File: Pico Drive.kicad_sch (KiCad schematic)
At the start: 23 parts, among them J1 Conn_01x06_Male, J2 Conn_01x08, J3 Conn_01x02_Male, J4 Conn_01x02_Male, SW1 Reset, U1 Pico, U2 74AXP1T45GWH, U3 74AHCT1G125, U4 OLED-I2C-Module-Aliexpress

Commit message: Shifted bits around, ran power, added cutout
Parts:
- added H1, H2, H3, H4: MountingHole, MountingHole:MountingHole_2.2mm_M2, symbol Mechanical:MountingHole
- SW1: footprint Button_Switch_THT:SW_PUSH-12mm -> Button_Switch_THT:SW_PUSH_6mm
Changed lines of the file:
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@@
     (pin "1")
+  )
+  (symbol (lib_id "Mechanical:MountingHole") (at 107.95 54.61 0) (unit 1)
+    (in_bom yes) (on_board yes) (fields_autoplaced)
+    (property "Reference" "H2" (id 0) (at 110.49 53.7753 0)
+      (effects (font (size 1.27 1.27)) (justify left))
+    )
+    (property "Value" "MountingHole" (id 1) (at 110.49 56.3122 0)
+      (effects (font (size 1.27 1.27)) (justify left))
+    )
+    (property "Footprint" "MountingHole:MountingHole_2.2mm_M2" (id 2) (at 107.95 54.61 0)
+      (effects (font (size 1.27 1.27)) hide)
+    )
+    (property "Datasheet" "~" (id 3) (at 107.95 54.61 0)
+      (effects (font (size 1.27 1.27)) hide)
+    )
   )
   (symbol (lib_id "power:GND") (at 71.12 57.15 90) (unit 1)
@@
     (pin "4")
   )
+  (symbol (lib_id "Mechanical:MountingHole") (at 88.9 54.61 0) (unit 1)
+    (in_bom yes) (on_board yes) (fields_autoplaced)
+    (property "Reference" "H1" (id 0) (at 91.44 53.7753 0)
+      (effects (font (size 1.27 1.27)) (justify left))
+    )
+    (property "Value" "MountingHole" (id 1) (at 91.44 56.3122 0)
+      (effects (font (size 1.27 1.27)) (justify left))
+    )
+    (property "Footprint" "MountingHole:MountingHole_2.2mm_M2" (id 2) (at 88.9 54.61 0)
+      (effects (font (size 1.27 1.27)) hide)
+    )
+    (property "Datasheet" "~" (id 3) (at 88.9 54.61 0)
+      (effects (font (size 1.27 1.27)) hide)
+    )
+  )
   (symbol (lib_id "Switch:SW_Push") (at 22.86 182.245 90) (unit 1)
     (in_bom yes) (on_board yes) (fields_autoplaced)
@@
       (effects (font (size 1.27 1.27)) (justify right))
     )
-    (property "Footprint" "Button_Switch_THT:SW_PUSH-12mm" (id 2) (at 17.78 182.245 0)
+    (property "Footprint" "Button_Switch_THT:SW_PUSH_6mm" (id 2) (at 17.78 182.245 0)
       (effects (font (size 1.27 1.27)) hide)
     )
@@
     (pin "1")
     (pin "2")
+  )
+  (symbol (lib_id "Mechanical:MountingHole") (at 88.9 59.69 0) (unit 1)
+    (in_bom yes) (on_board yes) (fields_autoplaced)
+    (property "Reference" "H3" (id 0) (at 91.44 58.8553 0)
+      (effects (font (size 1.27 1.27)) (justify left))
+    )
+    (property "Value" "MountingHole" (id 1) (at 91.44 61.3922 0)
+      (effects (font (size 1.27 1.27)) (justify left))
+    )
+    (property "Footprint" "MountingHole:MountingHole_2.2mm_M2" (id 2) (at 88.9 59.69 0)
+      (effects (font (size 1.27 1.27)) hide)
+    )
+    (property "Datasheet" "~" (id 3) (at 88.9 59.69 0)
+      (effects (font (size 1.27 1.27)) hide)
+    )
+  )
+  (symbol (lib_id "Mechanical:MountingHole") (at 107.95 59.69 0) (unit 1)
+    (in_bom yes) (on_board yes) (fields_autoplaced)
+    (property "Reference" "H4" (id 0) (at 110.49 58.8553 0)
+      (effects (font (size 1.27 1.27)) (justify left))
+    )
+    (property "Value" "MountingHole" (id 1) (at 110.49 61.3922 0)
+      (effects (font (size 1.27 1.27)) (justify left))
+    )
+    (property "Footprint" "MountingHole:MountingHole_2.2mm_M2" (id 2) (at 107.95 59.69 0)
+      (effects (font (size 1.27 1.27)) hide)
+    )
+    (property "Datasheet" "~" (id 3) (at 107.95 59.69 0)
+      (effects (font (size 1.27 1.27)) hide)
+    )
   )
   (symbol (lib_id "Connector_Generic:Conn_01x03") (at 35.56 97.79 0) (unit 1)
@@
       (reference "D1") (unit 1) (value "LED") (footprint "LED_THT:LED_D5.0mm")
     )
+    (path "/6aaac48c-1084-4417-a5ba-7ef20c482d61"
+      (reference "H1") (unit 1) (value "MountingHole") (footprint "MountingHole:MountingHole_2.2mm_M2")
+    )
+    (path "/36716edf-5df6-475e-8e31-d4be639e19ec"
+      (reference "H2") (unit 1) (value "MountingHole") (footprint "MountingHole:MountingHole_2.2mm_M2")
+    )
+    (path "/702feb10-b0c8-409f-9d53-2d411bf5bcd2"
+      (reference "H3") (unit 1) (value "MountingHole") (footprint "MountingHole:MountingHole_2.2mm_M2")
+    )
+    (path "/72a812fd-69d5-499a-ae49-86d7d93a117e"
+      (reference "H4") (unit 1) (value "MountingHole") (footprint "MountingHole:MountingHole_2.2mm_M2")
+    )
     (path "/39882caa-95f6-44aa-91c3-f39af783c8e6"
       (reference "J1") (unit 1) (value "Conn_01x06_Male") (footprint "Connector_PinHeader_2.54mm:PinHeader_1x06_P2.54mm_Horizontal")
@@
     )
     (path "/6c8f0377-4b1d-4b1f-8f24-8c0f143dd748"
-      (reference "SW1") (unit 1) (value "Reset") (footprint "Button_Switch_THT:SW_PUSH-12mm")
+      (reference "SW1") (unit 1) (value "Reset") (footprint "Button_Switch_THT:SW_PUSH_6mm")
     )
     (path "/ed3c498f-b044-4833-8009-2bc5c40e76df"

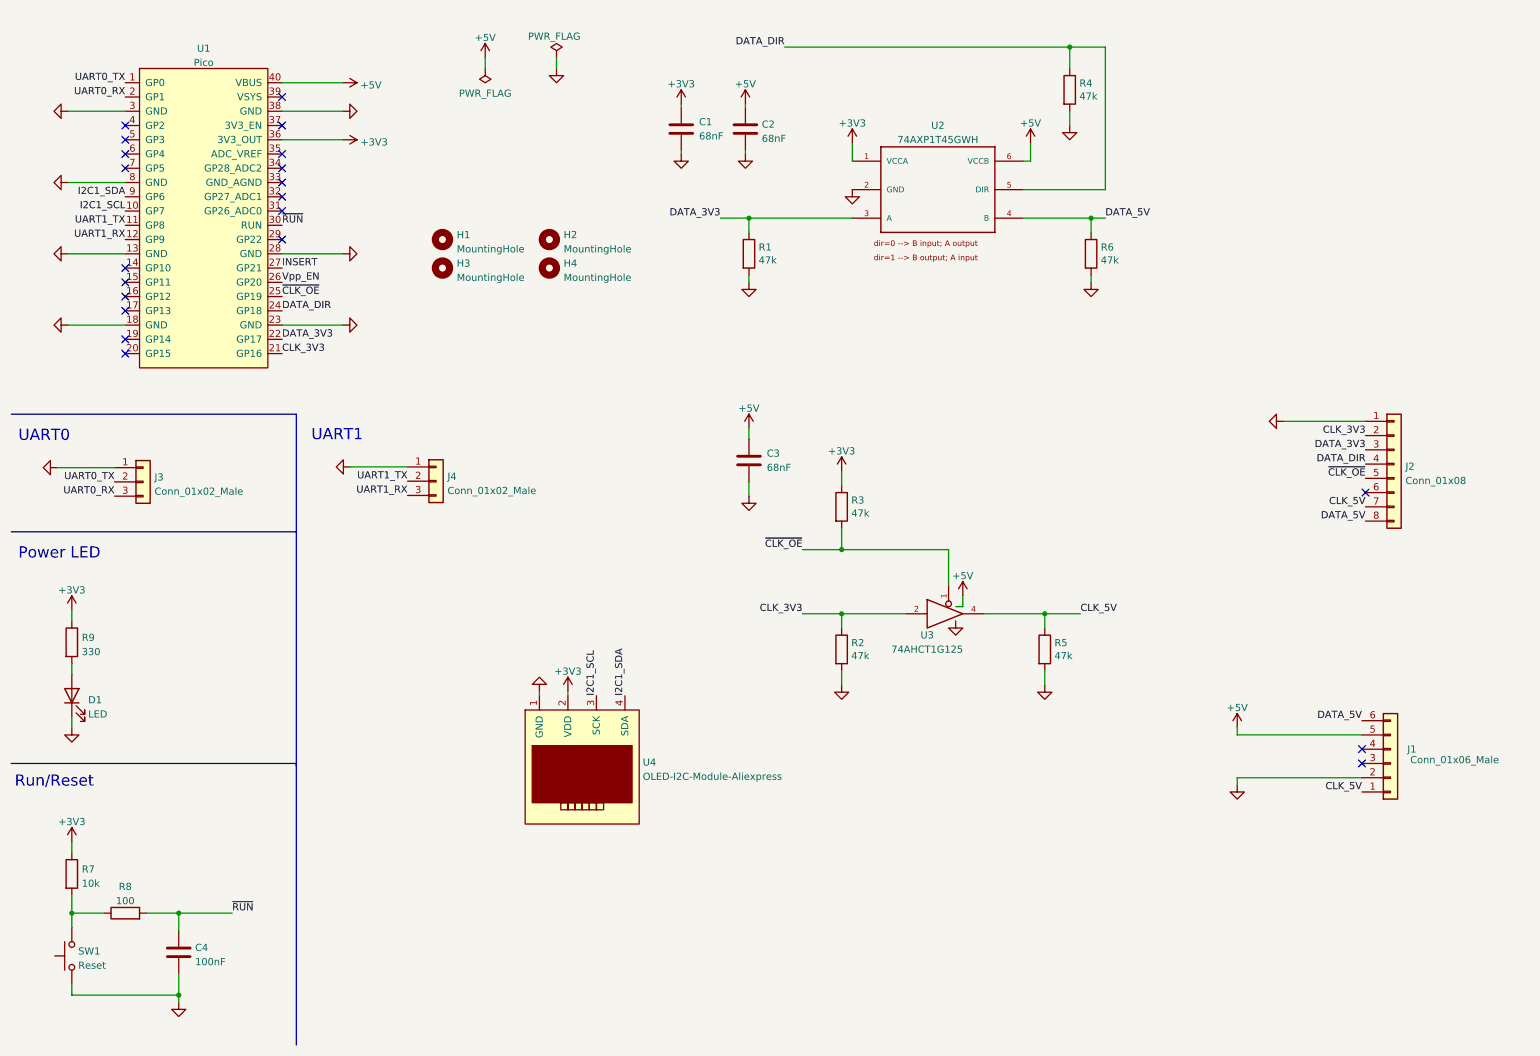
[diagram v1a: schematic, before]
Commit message: Swapped some TH for SMDs, fixed caps, tidied
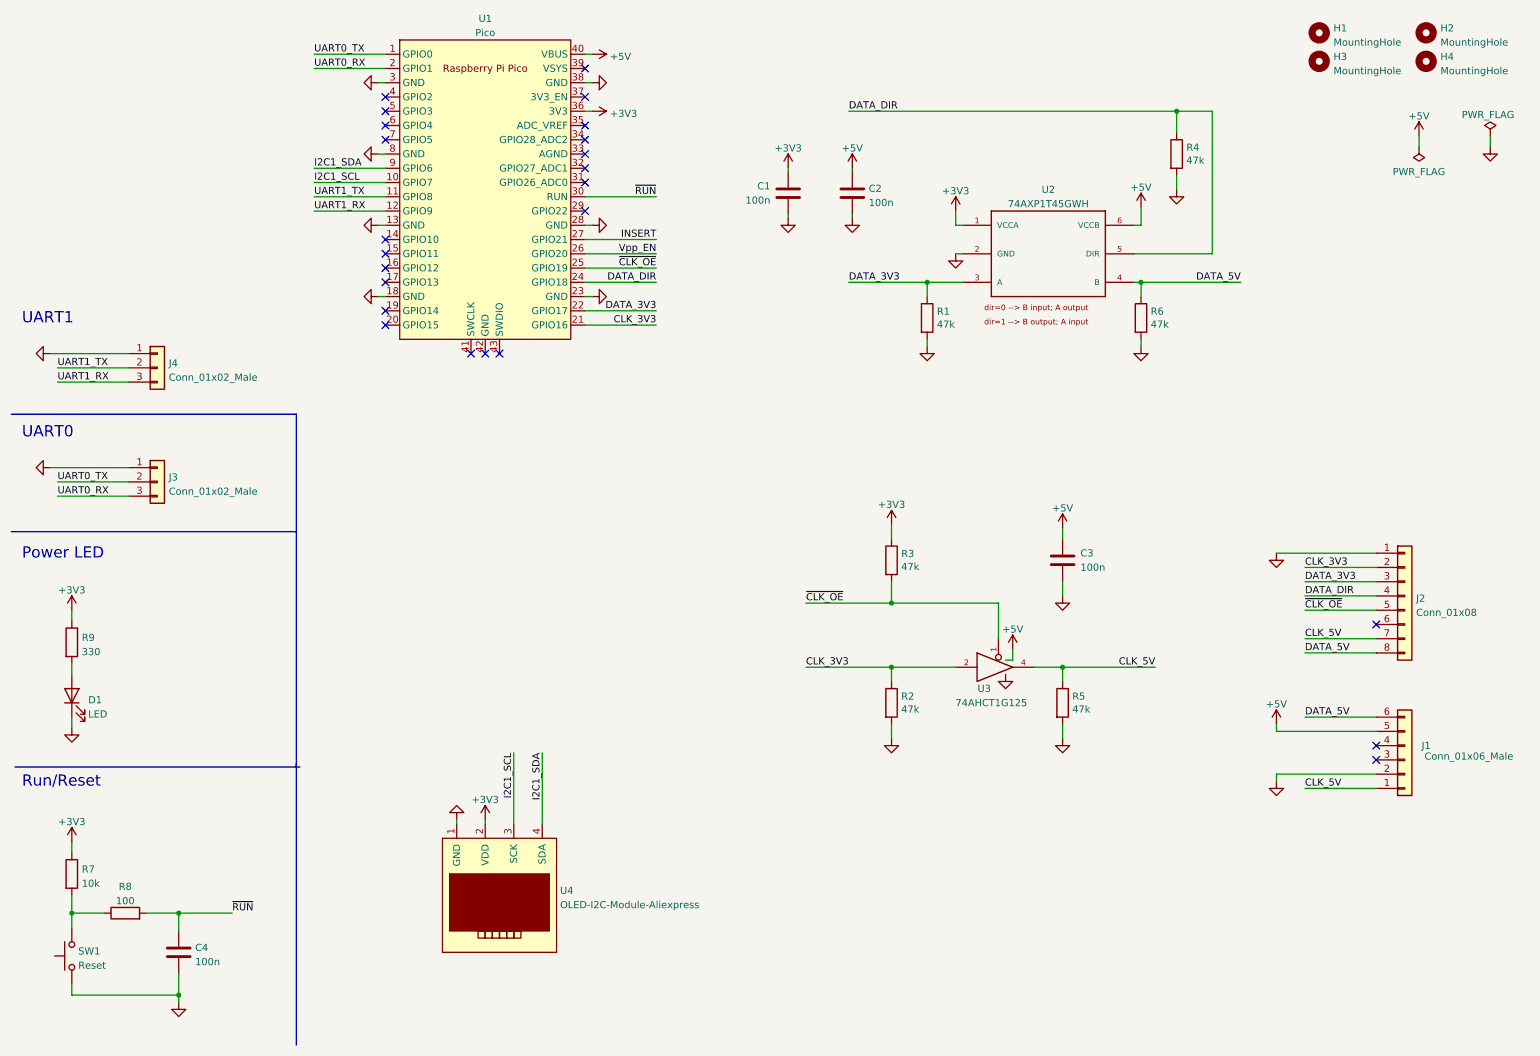
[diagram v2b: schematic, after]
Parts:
- removed U1: Pico, RPi_Pico:RPi_Pico_SMD_TH, symbol kiwih_kicad:raspberrypi-pico-module
- added U1: Pico, RP-Pico Libraries:RPi_Pico_SMD_TH, symbol MCU_RaspberryPi_and_Boards:Pico
- C1, C2, C3: value 68nF -> 100n; footprint Capacitor_THT:C_Disc_D4.3mm_W1.9mm_P5.00mm -> Capacitor_SMD:C_0402_1005Metric_Pad0.74x0.62mm_HandSolder
- C4: value 100nF -> 100n; footprint Capacitor_THT:C_Disc_D4.3mm_W1.9mm_P5.00mm -> Capacitor_SMD:C_0402_1005Metric_Pad0.74x0.62mm_HandSolder
- D1: footprint LED_THT:LED_D5.0mm -> LED_SMD:LED_0603_1608Metric_Pad1.05x0.95mm_HandSolder
- R1, R2, R3, R4, R5, R6, R7, R8, R9: footprint Resistor_THT:R_Axial_DIN0204_L3.6mm_D1.6mm_P7.62mm_Horizontal -> Resistor_SMD:R_0402_1005Metric_Pad0.72x0.64mm_HandSolder
- U2: footprint Package_DIP:DIP-6_W7.62mm_Socket -> Package_TO_SOT_SMD:SOT-23-6_Handsoldering
- U3: footprint Package_DIP:DIP-6_W7.62mm_Socket -> Package_TO_SOT_SMD:TSOT-23-5
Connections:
- net +3V3: now also U1.36 (3V3)
- net +5V: now also U1.40 (VBUS)
- net CLK_3V3: now also U1.21 (GPIO16)
- net DATA_3V3: now also U1.22 (GPIO17)
- net DATA_DIR: now also U1.24 (GPIO18)
- net GND: now also U1.13 (GND), U1.18 (GND), U1.23 (GND), U1.28 (GND), U1.3 (GND), U1.38 (GND), U1.8 (GND)
- net I2C1_SCL: now also U1.10 (GPIO7)
- net I2C1_SDA: now also U1.9 (GPIO6)
- net INSERT: now also U1.27 (GPIO21)
- net UART0_RX: now also U1.2 (GPIO1)
- net UART0_TX: now also U1.1 (GPIO0)
- net UART1_RX: now also U1.12 (GPIO9)
- net UART1_TX: now also U1.11 (GPIO8)
- net Vpp_EN: now also U1.26 (GPIO20)
- net ~{CLK_OE}: now also U1.25 (GPIO19)
- net ~{RUN}: now also U1.30 (RUN)
- no-connect marks 21 -> 24
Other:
- moved on the sheet: C1, C2, C3, H1, H2, H3, H4, J1, J2, J3, J4, R1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

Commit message: Rotated and shrank the board, tidied stuff up
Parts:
- J6: renamed from U4; value OLED-I2C-Module-Aliexpress -> I2C; footprint kiwih_kicad:OLED-I2C-Module-Aliexpress -> Connector_PinSocket_2.54mm:PinSocket_1x04_P2.54mm_Vertical; symbol kiwih_kicad:OLED-I2C-Module-Aliexpress -> Connector:Conn_01x04_Female
- SW1: footprint Button_Switch_THT:SW_PUSH_6mm -> digikey-footprints:Switch_Tactile_SMD_4.5x4.5mm_TL3315NF160Q
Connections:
- net +3V3: now also J6.3 (Pin_3); no longer J6.2 (VDD)
- net GND: now also J6.4 (Pin_4); no longer J6.1 (GND)
- net I2C1_SCL: now also J6.2 (Pin_2); no longer J6.3 (SCK)
- net I2C1_SDA: now also J6.1 (Pin_1); no longer J6.4 (SDA)
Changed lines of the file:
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@@
     (stroke (width 0) (type default) (color 0 0 0 0))
   )
-  (wire (pts (xy 101.6 146.05) (xy 101.6 158.75))
+  (wire (pts (xy 81.28 168.91) (xy 93.98 168.91))
     (stroke (width 0) (type default) (color 0 0 0 0))
   )
@@
     (stroke (width 0) (type default) (color 0 0 0 0))
   )
-  (wire (pts (xy 96.52 157.988) (xy 96.52 158.75))
+  (wire (pts (xy 76.2 171.45) (xy 93.98 171.45))
     (stroke (width 0) (type default) (color 0 0 0 0))
   )
@@
     (stroke (width 0) (type default) (color 0 0 0 0))
   )
-  (wire (pts (xy 91.44 157.988) (xy 91.44 158.75))
+  (wire (pts (xy 76.2 173.99) (xy 93.98 173.99))
     (stroke (width 0) (type default) (color 0 0 0 0))
   )
@@
     (stroke (width 0) (type default) (color 0 0 0 0))
   )
-  (wire (pts (xy 106.68 146.05) (xy 106.68 158.75))
+  (wire (pts (xy 81.28 166.37) (xy 93.98 166.37))
     (stroke (width 0) (type default) (color 0 0 0 0))
   )
@@
     (effects (font (size 1.27 1.27)) (justify left bottom))
   )
-  (label "I2C1_SCL" (at 101.6 146.05 270)
-    (effects (font (size 1.27 1.27)) (justify right bottom))
+  (label "I2C1_SCL" (at 81.28 168.91 0)
+    (effects (font (size 1.27 1.27)) (justify left bottom))
   )
   (label "~{RUN}" (at 51.435 174.625 0)
@@
     (effects (font (size 1.27 1.27)) (justify left bottom))
   )
-  (label "I2C1_SDA" (at 106.68 146.05 270)
-    (effects (font (size 1.27 1.27)) (justify right bottom))
+  (label "I2C1_SDA" (at 81.28 166.37 0)
+    (effects (font (size 1.27 1.27)) (justify left bottom))
   )
   (label "CLK_3V3" (at 153.67 130.81 0)
@@
     (pin "1")
   )
-  (symbol (lib_id "power:GND") (at 91.44 157.988 180) (unit 1)
-    (in_bom yes) (on_board yes) (fields_autoplaced)
-    (property "Reference" "#PWR0138" (id 0) (at 91.44 151.638 0)
-      (effects (font (size 1.27 1.27)) hide)
-    )
-    (property "Value" "GND" (id 1) (at 91.0062 154.8131 90)
+  (symbol (lib_id "power:GND") (at 76.2 173.99 0) (unit 1)
+    (in_bom yes) (on_board yes) (fields_autoplaced)
+    (property "Reference" "#PWR0138" (id 0) (at 76.2 180.34 0)
+      (effects (font (size 1.27 1.27)) hide)
+    )
+    (property "Value" "GND" (id 1) (at 76.6338 177.1649 90)
       (effects (font (size 1.27 1.27)) (justify right) hide)
     )
-    (property "Footprint" "" (id 2) (at 91.44 157.988 0)
-      (effects (font (size 1.27 1.27)) hide)
-    )
-    (property "Datasheet" "" (id 3) (at 91.44 157.988 0)
+    (property "Footprint" "" (id 2) (at 76.2 173.99 0)
+      (effects (font (size 1.27 1.27)) hide)
+    )
+    (property "Datasheet" "" (id 3) (at 76.2 173.99 0)
       (effects (font (size 1.27 1.27)) hide)
     )
@@
     (pin "1")
   )
-  (symbol (lib_id "kiwih_kicad:OLED-I2C-Module-Aliexpress") (at 99.06 168.91 0) (unit 1)
-    (in_bom yes) (on_board yes) (fields_autoplaced)
-    (property "Reference" "U4" (id 0) (at 109.855 170.6153 0)
-      (effects (font (size 1.27 1.27)) (justify left))
-    )
-    (property "Value" "OLED-I2C-Module-Aliexpress" (id 1) (at 109.855 173.1522 0)
-      (effects (font (size 1.27 1.27)) (justify left))
-    )
-    (property "Footprint" "kiwih_kicad:OLED-I2C-Module-Aliexpress" (id 2) (at 99.06 182.88 0)
-      (effects (font (size 1.27 1.27)) hide)
-    )
-    (property "Datasheet" "" (id 3) (at 99.06 182.88 0)
+  (symbol (lib_id "Connector:Conn_01x04_Female") (at 99.06 168.91 0) (unit 1)
+    (in_bom yes) (on_board yes) (fields_autoplaced)
+    (property "Reference" "J6" (id 0) (at 99.7712 169.3453 0)
+      (effects (font (size 1.27 1.27)) (justify left))
+    )
+    (property "Value" "I2C" (id 1) (at 99.7712 171.8822 0)
+      (effects (font (size 1.27 1.27)) (justify left))
+    )
+    (property "Footprint" "Connector_PinSocket_2.54mm:PinSocket_1x04_P2.54mm_Vertical" (id 2) (at 99.06 168.91 0)
+      (effects (font (size 1.27 1.27)) hide)
+    )
+    (property "Datasheet" "~" (id 3) (at 99.06 168.91 0)
       (effects (font (size 1.27 1.27)) hide)
     )
@@
       (effects (font (size 1.27 1.27)) (justify right))
     )
-    (property "Footprint" "Button_Switch_THT:SW_PUSH_6mm" (id 2) (at 17.78 182.245 0)
+    (property "Footprint" "digikey-footprints:Switch_Tactile_SMD_4.5x4.5mm_TL3315NF160Q" (id 2) (at 17.78 182.245 0)
       (effects (font (size 1.27 1.27)) hide)
     )
@@
     (pin "1")
   )
-  (symbol (lib_id "power:+3V3") (at 96.52 157.988 0) (unit 1)
-    (in_bom yes) (on_board yes)
-    (property "Reference" "#PWR0139" (id 0) (at 96.52 161.798 0)
-      (effects (font (size 1.27 1.27)) hide)
-    )
-    (property "Value" "+3V3" (id 1) (at 96.52 154.4122 0))
-    (property "Footprint" "" (id 2) (at 96.52 157.988 0)
-      (effects (font (size 1.27 1.27)) hide)
-    )
-    (property "Datasheet" "" (id 3) (at 96.52 157.988 0)
+  (symbol (lib_id "power:+3V3") (at 76.2 171.45 0) (unit 1)
+    (in_bom yes) (on_board yes)
+    (property "Reference" "#PWR0139" (id 0) (at 76.2 175.26 0)
+      (effects (font (size 1.27 1.27)) hide)
+    )
+    (property "Value" "+3V3" (id 1) (at 76.2 167.8742 0))
+    (property "Footprint" "" (id 2) (at 76.2 171.45 0)
+      (effects (font (size 1.27 1.27)) hide)
+    )
+    (property "Datasheet" "" (id 3) (at 76.2 171.45 0)
       (effects (font (size 1.27 1.27)) hide)
     )
@@
       (reference "J4") (unit 1) (value "Conn_01x02_Male") (footprint "Connector_PinHeader_2.54mm:PinHeader_1x03_P2.54mm_Vertical")
     )
+    (path "/69b2bf00-5a84-4293-8b76-150c238a544b"
+      (reference "J6") (unit 1) (value "I2C") (footprint "Connector_PinSocket_2.54mm:PinSocket_1x04_P2.54mm_Vertical")
+    )
     (path "/a7fba6d8-15b2-4964-b8ff-6759b53d0973"
       (reference "R1") (unit 1) (value "47k") (footprint "Resistor_SMD:R_0402_1005Metric_Pad0.72x0.64mm_HandSolder")
@@
     )
     (path "/6c8f0377-4b1d-4b1f-8f24-8c0f143dd748"
-      (reference "SW1") (unit 1) (value "Reset") (footprint "Button_Switch_THT:SW_PUSH_6mm")
+      (reference "SW1") (unit 1) (value "Reset") (footprint "digikey-footprints:Switch_Tactile_SMD_4.5x4.5mm_TL3315NF160Q")
     )
     (path "/04ac89cb-82bd-493c-b55f-dcdc4402b033"
@@
       (reference "U3") (unit 1) (value "74AHCT1G125") (footprint "Package_TO_SOT_SMD:TSOT-23-5")
     )
-    (path "/69b2bf00-5a84-4293-8b76-150c238a544b"
-      (reference "U4") (unit 1) (value "OLED-I2C-Module-Aliexpress") (footprint "kiwih_kicad:OLED-I2C-Module-Aliexpress")
-    )
-  )
+  )

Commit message: Complete revamp, with routing.
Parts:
- removed J4: Conn_01x02_Male, Connector_PinHeader_2.54mm:PinHeader_1x03_P2.54mm_Vertical, symbol Connector_Generic:Conn_01x03
- added J4: Conn_01x06, Connector_PinSocket_2.54mm:PinSocket_1x06_P2.54mm_Vertical, symbol Connector_Generic:Conn_01x06
- J1: footprint Connector_PinHeader_2.54mm:PinHeader_1x06_P2.54mm_Horizontal -> Connector_PinHeader_2.54mm:PinHeader_1x06_P2.54mm_Vertical
- J2: value Conn_01x08 -> Conn_01x05; footprint Connector_PinSocket_2.54mm:PinSocket_1x08_P2.54mm_Vertical -> Connector_PinSocket_2.54mm:PinSocket_1x05_P2.54mm_Vertical; symbol Connector_Generic:Conn_01x08 -> Connector_Generic:Conn_01x05
- J3: value Conn_01x02_Male -> Conn_01x03_Male
- U3: value 74AHCT1G125 -> 74AHCT1G125DBVTG4
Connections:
- net +5V: now also J1.3 (Pin_3), J4.3 (Pin_3), J4.5 (Pin_5)
- net CLK_5V: now also J4.1 (Pin_1); no longer J2.7 (Pin_7)
- net DATA_3V3: now also J2.5 (Pin_5), U1.25 (GPIO19); no longer J2.3 (Pin_3), U1.22 (GPIO17)
- net DATA_5V: now also J4.6 (Pin_6); no longer J2.8 (Pin_8)
- net GND: now also J4.2 (Pin_2)
- net ~{CLK_OE}: now also J2.3 (Pin_3), U1.22 (GPIO17); no longer J2.5 (Pin_5), U1.25 (GPIO19)
- net VDD: now reaches J1.4 (Pin_4)
- net VDD: now also J4.4 (Pin_4)
- no-connect marks 24 -> 21
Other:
- note removed: "UART1"
- moved on the sheet: J1

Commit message: Moved R3, changed U2 for SOT363, various fixes
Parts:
- U2: footprint Package_TO_SOT_SMD:SOT-23-6_Handsoldering -> Package_TO_SOT_SMD:SOT-363_SC-70-6_Handsoldering
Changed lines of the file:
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@@
       (effects (font (size 1.27 1.27)))
     )
-    (property "Footprint" "Package_TO_SOT_SMD:SOT-23-6_Handsoldering" (at 186.69 49.53 0)
+    (property "Footprint" "Package_TO_SOT_SMD:SOT-363_SC-70-6_Handsoldering" (at 186.69 49.53 0)
       (effects (font (size 1.27 1.27)) (justify left bottom) hide)
     )
